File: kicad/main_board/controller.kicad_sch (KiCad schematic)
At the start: 46 parts, among them J1 FRONT_PANEL, J2 I2C, J3 SWD, U1 MCP4728, U2 RP2040, U3 W25Q128JVP, Y1 12MHz

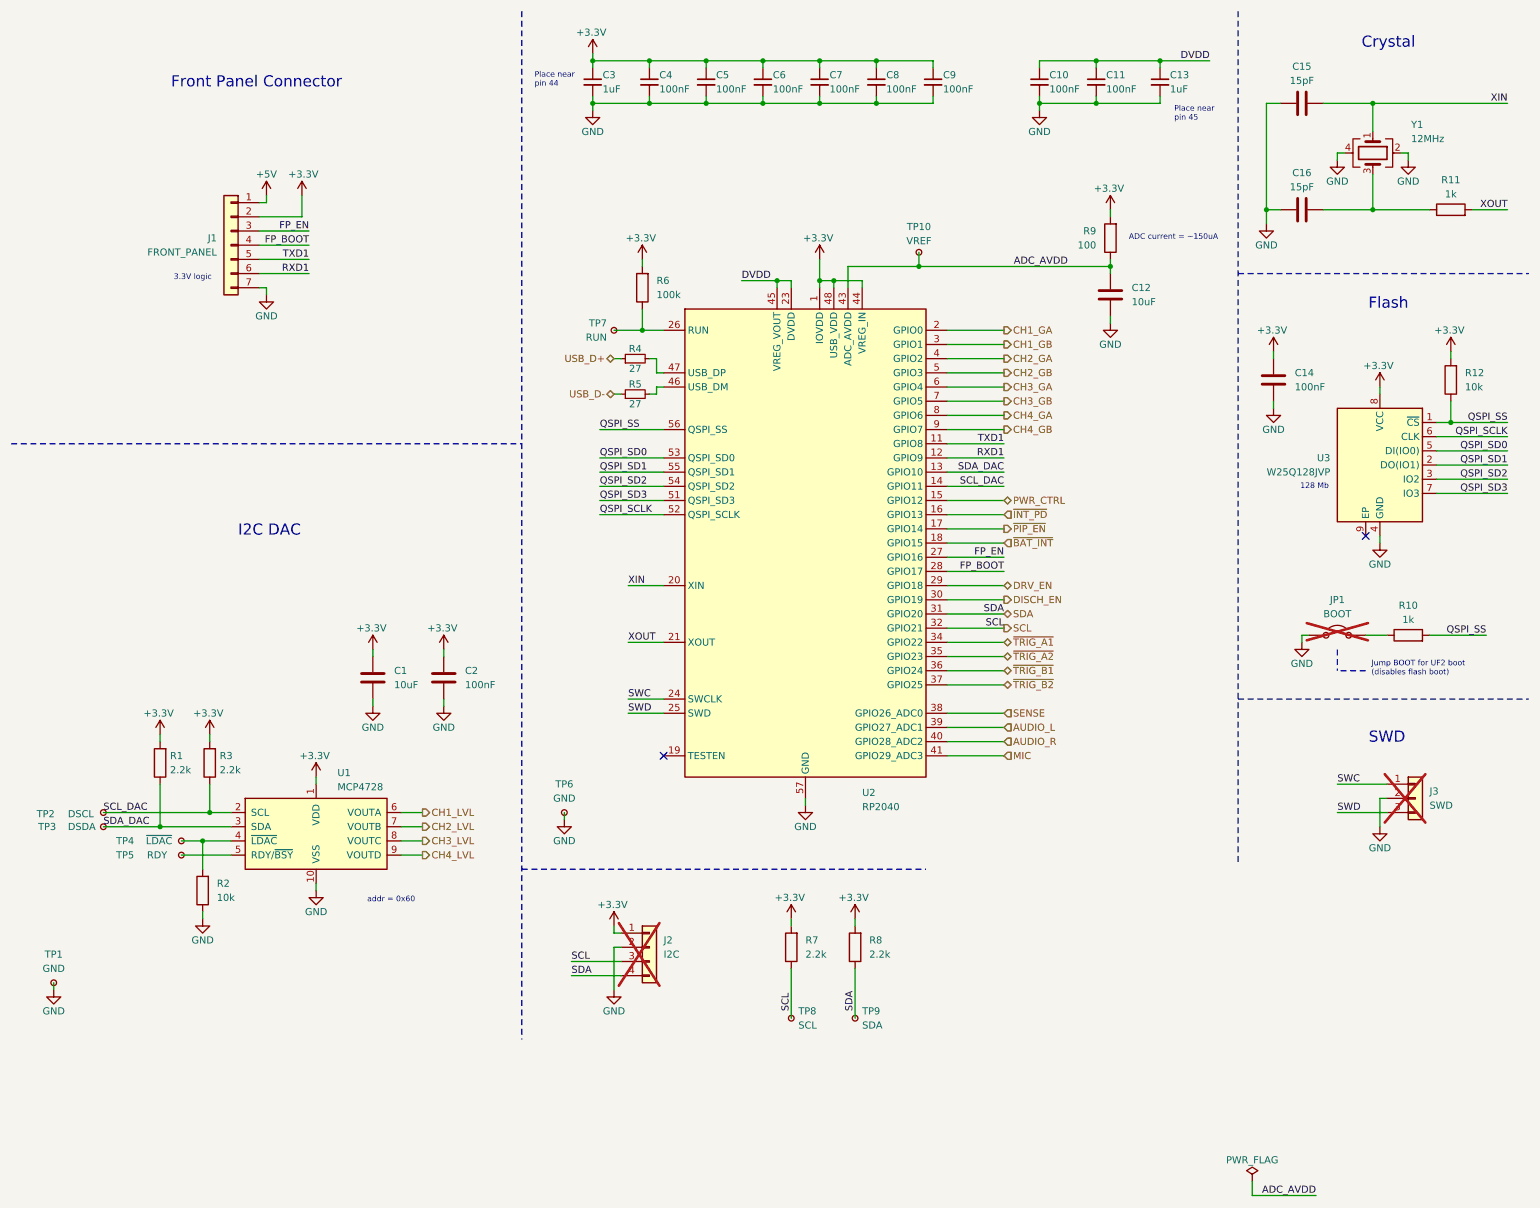
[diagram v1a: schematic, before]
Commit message: add input
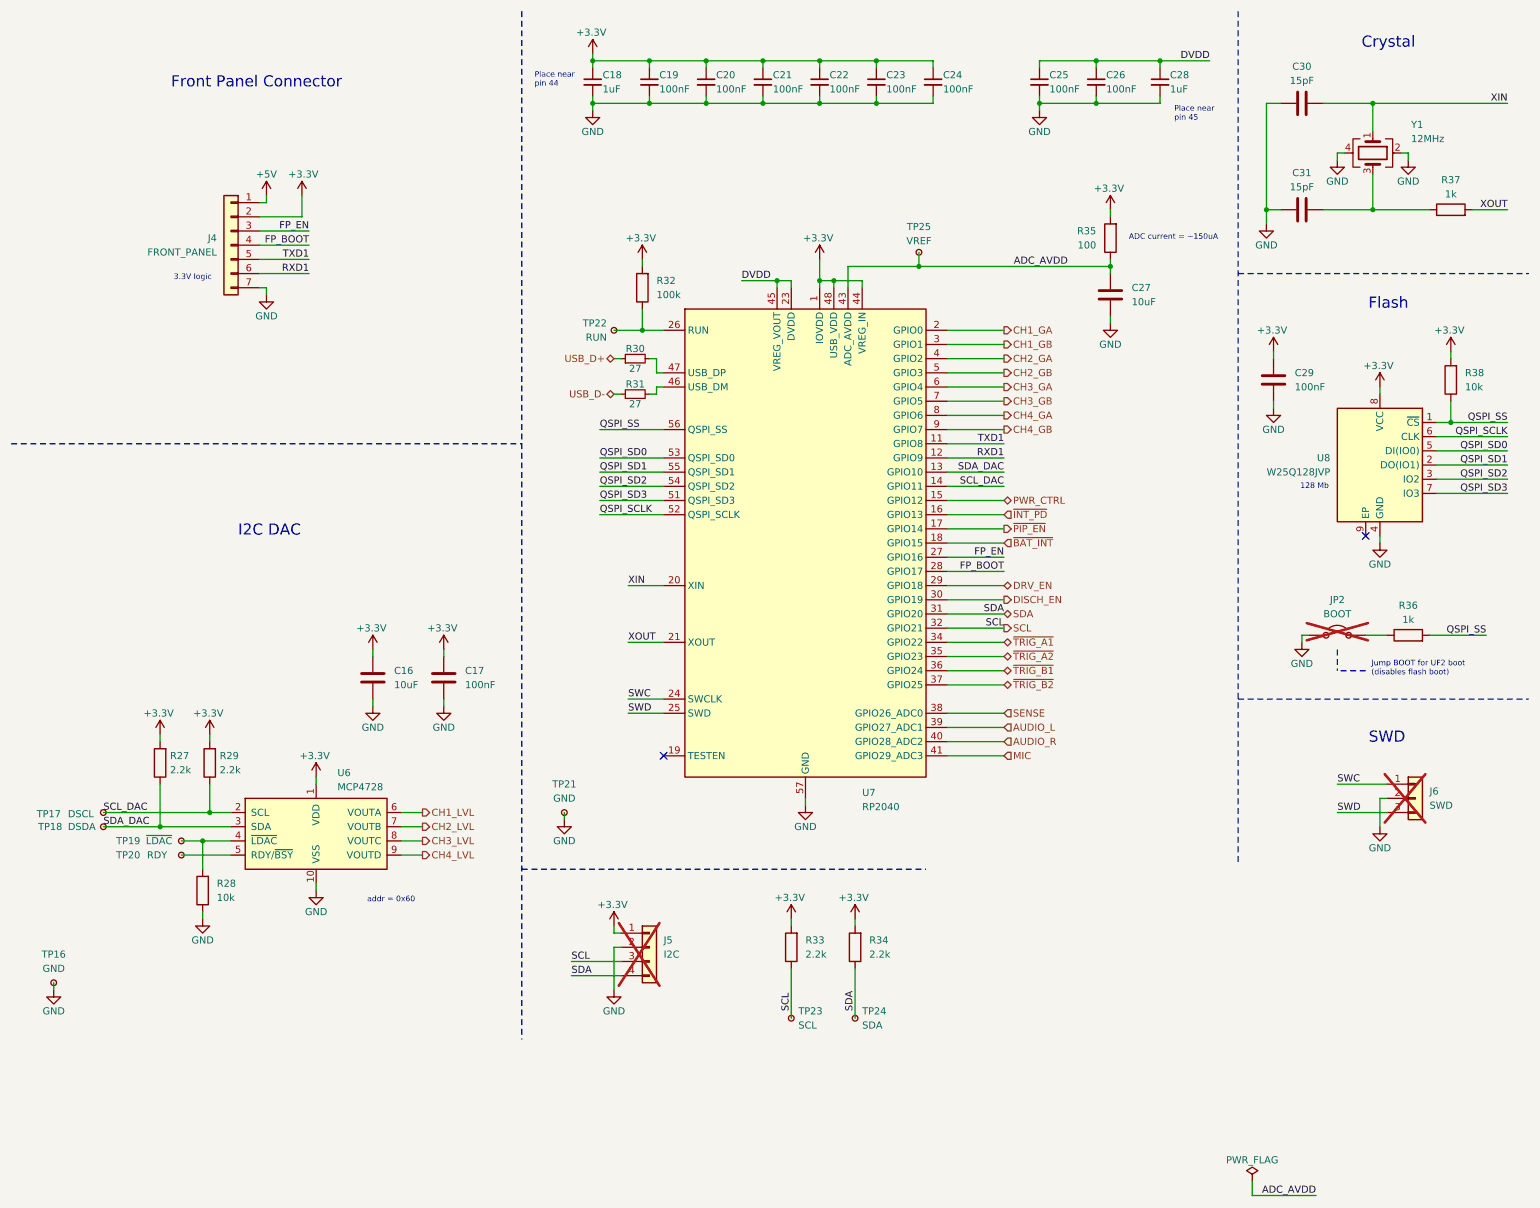
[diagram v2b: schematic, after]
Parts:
- renumbered C1 to C16, C2 to C17, C3 to C18, C4 to C19, C5 to C20, C6 to C21, C7 to C22, C8 to C23, C9 to C24, C10 to C25, C11 to C26, C12 to C27, C13 to C28, C14 to C29, C15 to C30, C16 to C31, J1 to J4, J2 to J5, J3 to J6, JP1 to JP2, R1 to R27, R2 to R28, R3 to R29, R4 to R30, R5 to R31, R6 to R32, R7 to R33, R8 to R34, R9 to R35, R10 to R36, R11 to R37, R12 to R38, TP1 to TP16, TP2 to TP17, TP3 to TP18, TP4 to TP19, TP5 to TP20, TP6 to TP21, TP7 to TP22, TP8 to TP23, TP9 to TP24, TP10 to TP25, U1 to U6, U2 to U7, U3 to U8

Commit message: add audio
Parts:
- renumbered TP16 to TP15, TP17 to TP16, TP18 to TP17, TP19 to TP18, TP20 to TP19, TP21 to TP20, TP22 to TP21, TP23 to TP22, TP24 to TP23, TP25 to TP24
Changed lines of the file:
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@@
 		(on_board yes)
 		(dnp no)
-		(property "Reference" "TP20"
+		(property "Reference" "TP19"
 			(at 31.496 163.83 0)
 			(effects
@@
 			(project "main_board"
 				(path "/8e1f1504-76c2-49e6-9261-3c1190503f8c/c17fbfa0-81d7-4817-8752-da6de21e6518"
-					(reference "TP20")
+					(reference "TP19")
 					(unit 1)
 				)
@@
 		(on_board yes)
 		(dnp no)
-		(property "Reference" "TP18"
+		(property "Reference" "TP17"
 			(at 17.526 158.75 0)
 			(effects
@@
 			(project "main_board"
 				(path "/8e1f1504-76c2-49e6-9261-3c1190503f8c/c17fbfa0-81d7-4817-8752-da6de21e6518"
-					(reference "TP18")
+					(reference "TP17")
 					(unit 1)
 				)
@@
 		(dnp no)
 		(fields_autoplaced yes)
-		(property "Reference" "TP24"
+		(property "Reference" "TP23"
 			(at 165.1 191.7699 0)
 			(effects
@@
 			(project "main_board"
 				(path "/8e1f1504-76c2-49e6-9261-3c1190503f8c/c17fbfa0-81d7-4817-8752-da6de21e6518"
-					(reference "TP24")
+					(reference "TP23")
 					(unit 1)
 				)
@@
 		(on_board yes)
 		(dnp no)
-		(property "Reference" "TP19"
+		(property "Reference" "TP18"
 			(at 31.496 161.29 0)
 			(effects
@@
 			(project "main_board"
 				(path "/8e1f1504-76c2-49e6-9261-3c1190503f8c/c17fbfa0-81d7-4817-8752-da6de21e6518"
-					(reference "TP19")
+					(reference "TP18")
 					(unit 1)
 				)
@@
 		(dnp no)
 		(fields_autoplaced yes)
-		(property "Reference" "TP22"
+		(property "Reference" "TP21"
 			(at 119.38 68.5799 0)
 			(effects
@@
 			(project "main_board"
 				(path "/8e1f1504-76c2-49e6-9261-3c1190503f8c/c17fbfa0-81d7-4817-8752-da6de21e6518"
-					(reference "TP22")
+					(reference "TP21")
 					(unit 1)
 				)
@@
 		(dnp no)
 		(fields_autoplaced yes)
-		(property "Reference" "TP23"
+		(property "Reference" "TP22"
 			(at 153.67 191.7699 0)
 			(effects
@@
 			(project "main_board"
 				(path "/8e1f1504-76c2-49e6-9261-3c1190503f8c/c17fbfa0-81d7-4817-8752-da6de21e6518"
-					(reference "TP23")
+					(reference "TP22")
 					(unit 1)
 				)
@@
 		(on_board yes)
 		(dnp no)
-		(property "Reference" "TP17"
+		(property "Reference" "TP16"
 			(at 17.272 156.464 0)
 			(effects
@@
 			(project "main_board"
 				(path "/8e1f1504-76c2-49e6-9261-3c1190503f8c/c17fbfa0-81d7-4817-8752-da6de21e6518"
-					(reference "TP17")
+					(reference "TP16")
 					(unit 1)
 				)
@@
 		(dnp no)
 		(fields_autoplaced yes)
-		(property "Reference" "TP21"
+		(property "Reference" "TP20"
 			(at 111.76 151.13 0)
 			(effects
@@
 			(project "main_board"
 				(path "/8e1f1504-76c2-49e6-9261-3c1190503f8c/c17fbfa0-81d7-4817-8752-da6de21e6518"
-					(reference "TP21")
+					(reference "TP20")
 					(unit 1)
 				)
@@
 		(dnp no)
 		(fields_autoplaced yes)
-		(property "Reference" "TP16"
+		(property "Reference" "TP15"
 			(at 20.32 181.61 0)
 			(effects
@@
 			(project "main_board"
 				(path "/8e1f1504-76c2-49e6-9261-3c1190503f8c/c17fbfa0-81d7-4817-8752-da6de21e6518"
-					(reference "TP16")
+					(reference "TP15")
 					(unit 1)
 				)
@@
 		(on_board yes)
 		(dnp no)
-		(property "Reference" "TP25"
+		(property "Reference" "TP24"
 			(at 175.26 51.308 0)
 			(effects
@@
 			(project "main_board"
 				(path "/8e1f1504-76c2-49e6-9261-3c1190503f8c/c17fbfa0-81d7-4817-8752-da6de21e6518"
-					(reference "TP25")
+					(reference "TP24")
 					(unit 1)
 				)

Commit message: add charger
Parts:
- renumbered C16 to C51, C17 to C52, C18 to C53, C19 to C54, C20 to C55, C21 to C56, C22 to C57, C23 to C58, C24 to C59, C25 to C60, C26 to C61, C27 to C62, C28 to C63, C29 to C64, C30 to C65, C31 to C66, J4 to J6, J5 to J7, J6 to J8, JP2 to JP3, R27 to R46, R28 to R47, R29 to R48, R30 to R49, R31 to R50, R32 to R51, R33 to R52, R34 to R53, R35 to R54, R36 to R55, R37 to R56, R38 to R57, TP15 to TP22, TP16 to TP23, TP17 to TP24, TP18 to TP25, TP19 to TP26, TP20 to TP27, TP21 to TP28, TP22 to TP29, TP23 to TP30, TP24 to TP31, U6 to U7, U7 to U8, U8 to U9

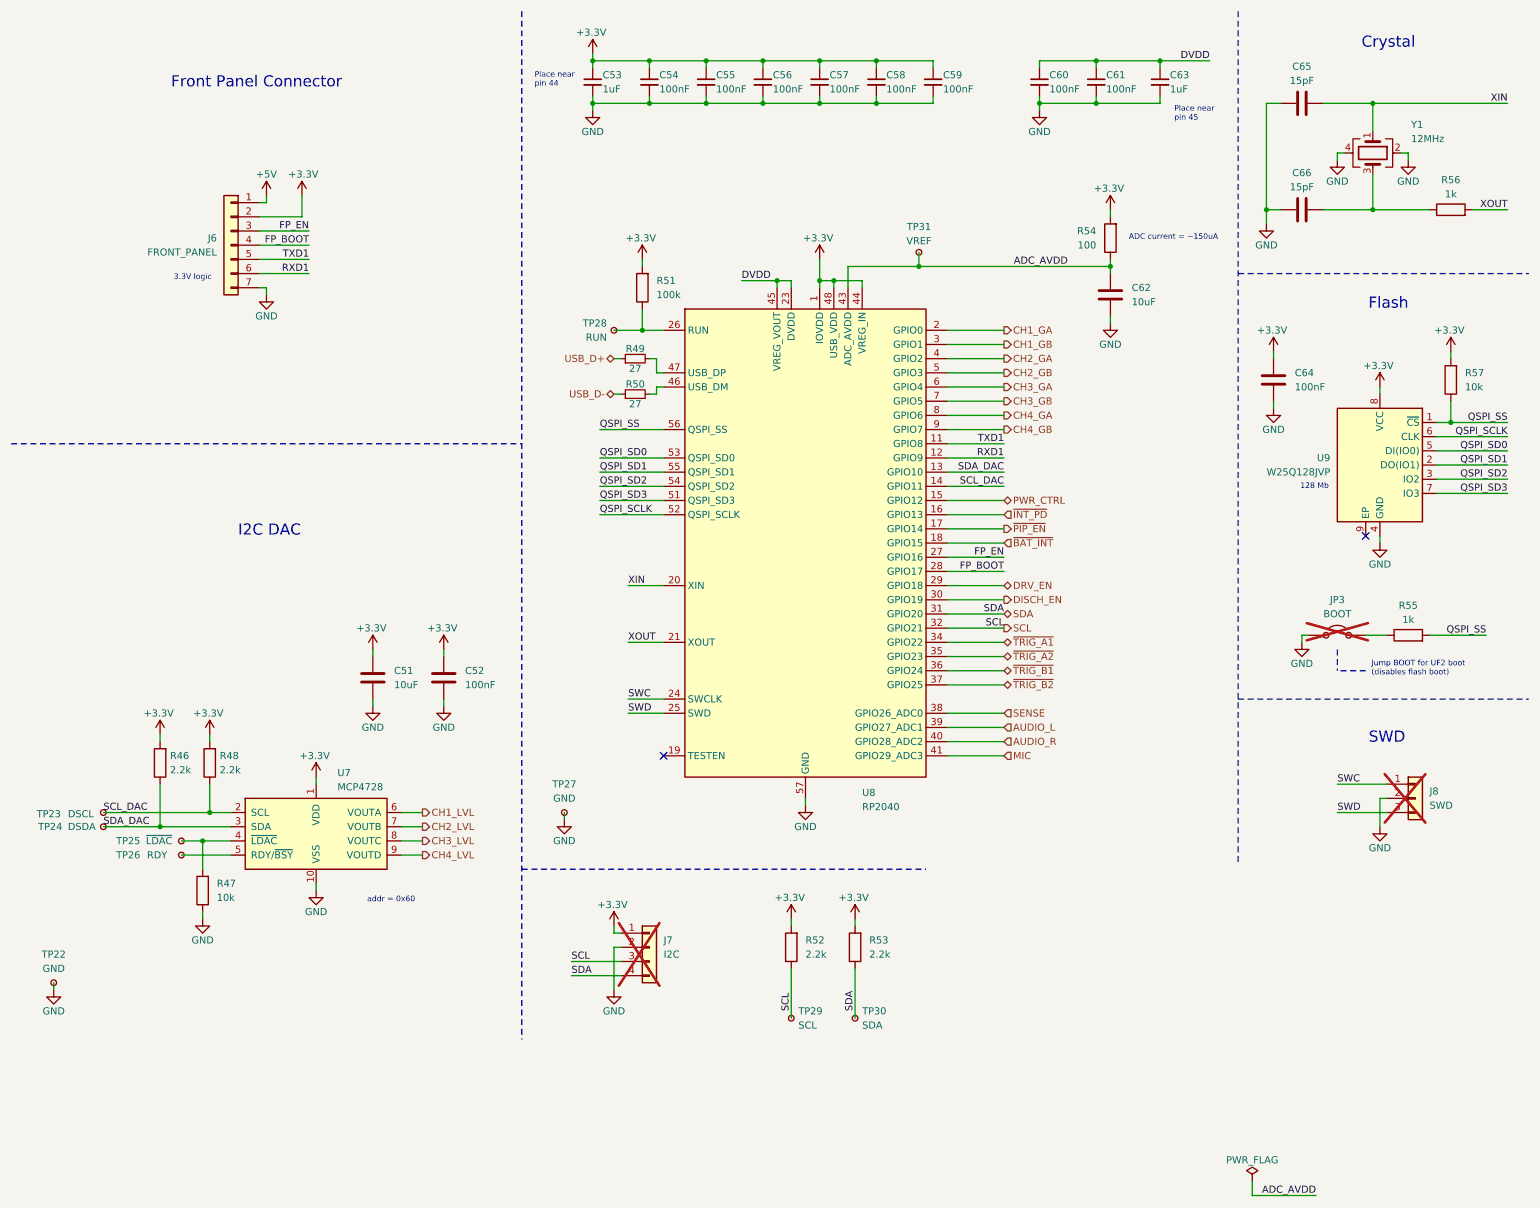
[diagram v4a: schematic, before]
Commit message: add I2S link
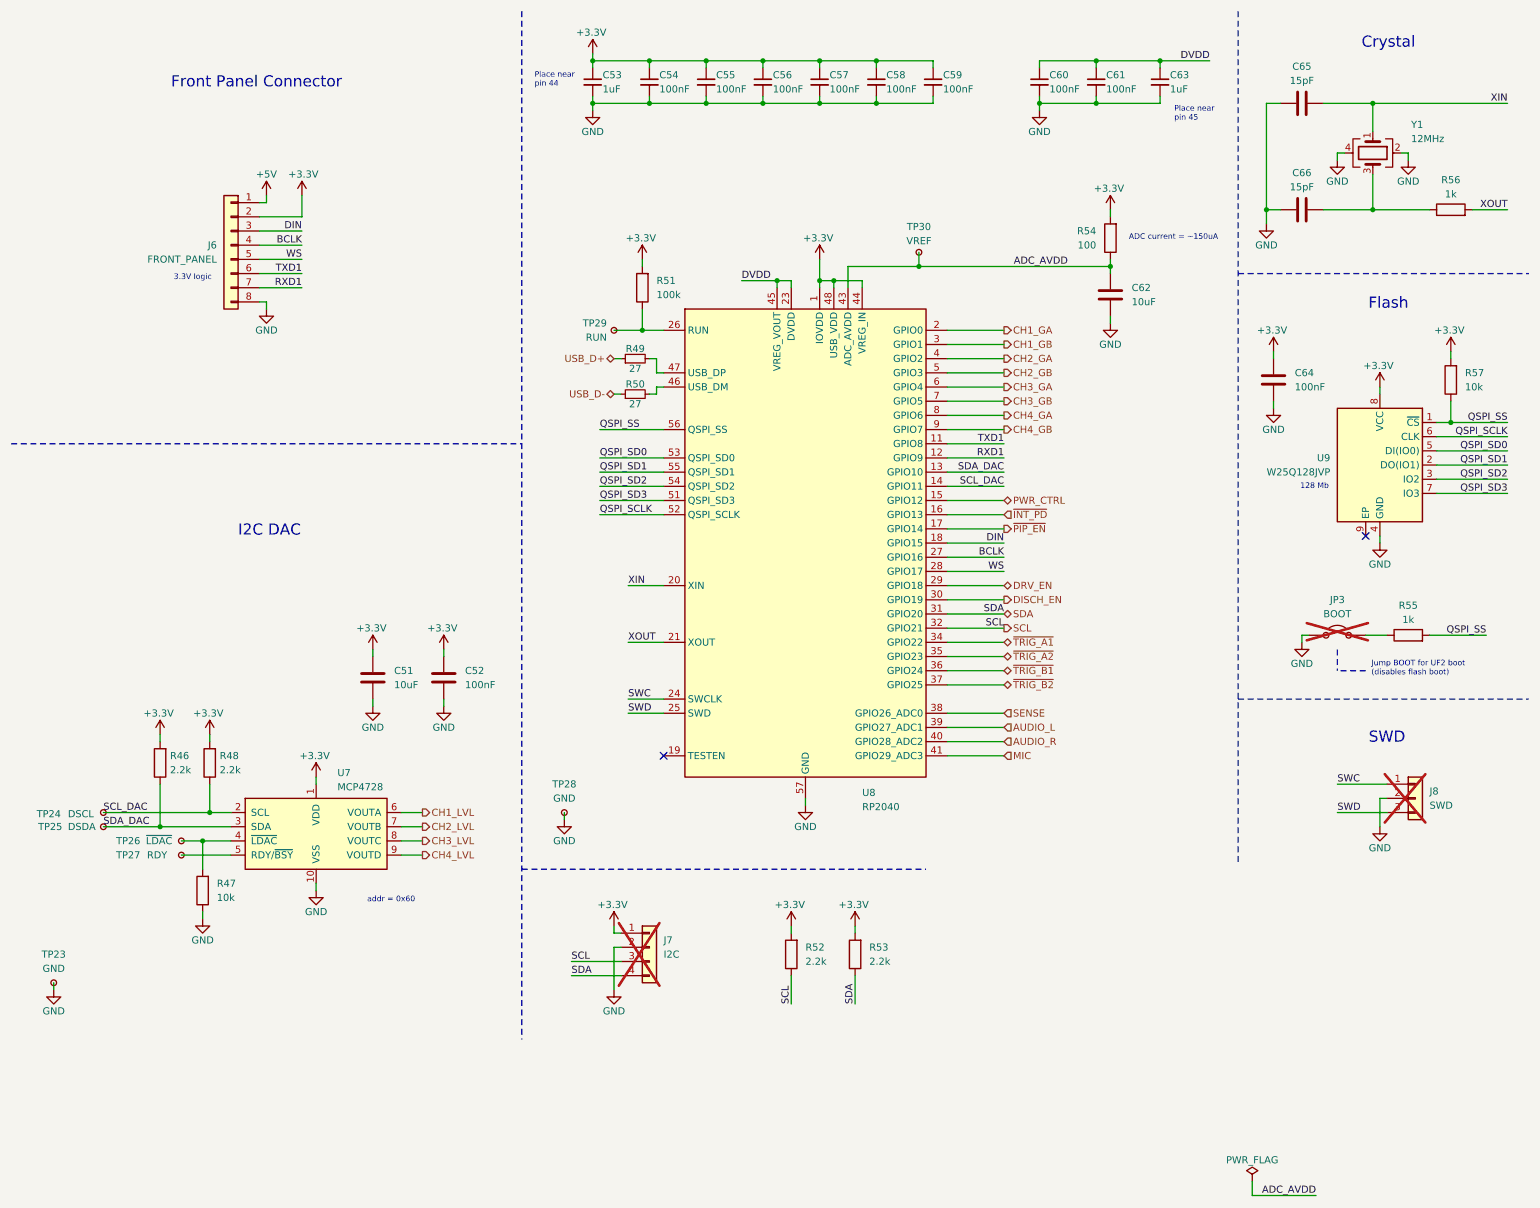
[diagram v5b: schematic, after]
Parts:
- removed TP29: SCL, TestPoint:TestPoint_Pad_D1.0mm, symbol Connector:TestPoint_Small
- removed TP30: SDA, TestPoint:TestPoint_Pad_D1.0mm, symbol Connector:TestPoint_Small
- J6: footprint Connector_JST:JST_PH_B8B-PH-K_1x07_P2.00mm_Vertical -> Connector_JST:JST_PH_B8B-PH-K_1x08_P2.00mm_Vertical; symbol Connector_Generic:Conn_01x07 -> Connector_Generic:Conn_01x08
- renumbered TP22 to TP23, TP23 to TP24, TP24 to TP25, TP25 to TP26, TP26 to TP27, TP27 to TP28, TP28 to TP29, TP31 to TP30
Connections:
- net ~{BAT_INT} is gone; now on net DIN: U8.18 (GPIO15)
- net GND: now also J6.8 (Pin_8); no longer J6.7 (Pin_7)
- net RXD1: now also J6.7 (Pin_7); no longer J6.6 (Pin_6)
- net TXD1: now also J6.6 (Pin_6); no longer J6.5 (Pin_5)
- net FP_BOOT renamed BCLK
- net BCLK: now also U8.27 (GPIO16); no longer U8.28 (GPIO17)
- net FP_EN renamed DIN
- net DIN: no longer U8.27 (GPIO16)
- new net WS: J6.5 (Pin_5), U8.28 (GPIO17)
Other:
- moved on the sheet: R52, R53
